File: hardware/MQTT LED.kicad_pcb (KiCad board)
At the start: 2 copper layers, 30 x 40 mm, 21 parts, among them J1 1x2P, J2 1x8P, J3 USB-TYPE-C-009, U1 ESPC2-M1-N2, U2 AL8860QMP-13, U3 AMS1117-3.3

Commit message: added todos
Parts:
- moved D1 6.34 mm to (122.2, 74.1), turned to 0 degrees
- moved L1 4.18 mm to (122.3, 81.3)
- moved R1 1.47 mm to (115.8, 71.4)
- moved J3 1.47 mm to (115.0, 77.5)
- moved R2 1.47 mm to (115.8, 83.5)
- moved C3 1.17 mm to (129.1, 84.4)
- moved U2 1.17 mm to (130.0, 81.5)
- moved R3 1.17 mm to (129.5, 87.1)
- moved J1 0.56 mm to (136.1, 81.0)
- moved C2 0.23 mm to (119.3, 61.8), turned to 90 degrees
- moved C4 0.12 mm to (119.4, 68.2)
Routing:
- net VBUS: track 45.7 -> 35.8 mm
- net +3V3: track 19.0 -> 16.2 mm
- net GND: track 31.0 -> 28.2 mm
- net LED-: track 21.7 -> 19.2 mm
- net LED+: track 9.65 -> 11.4 mm
- net Net-(D1-A): track 11.6 -> 12.5 mm
- net CTRL: track 12.8 -> 13.5 mm

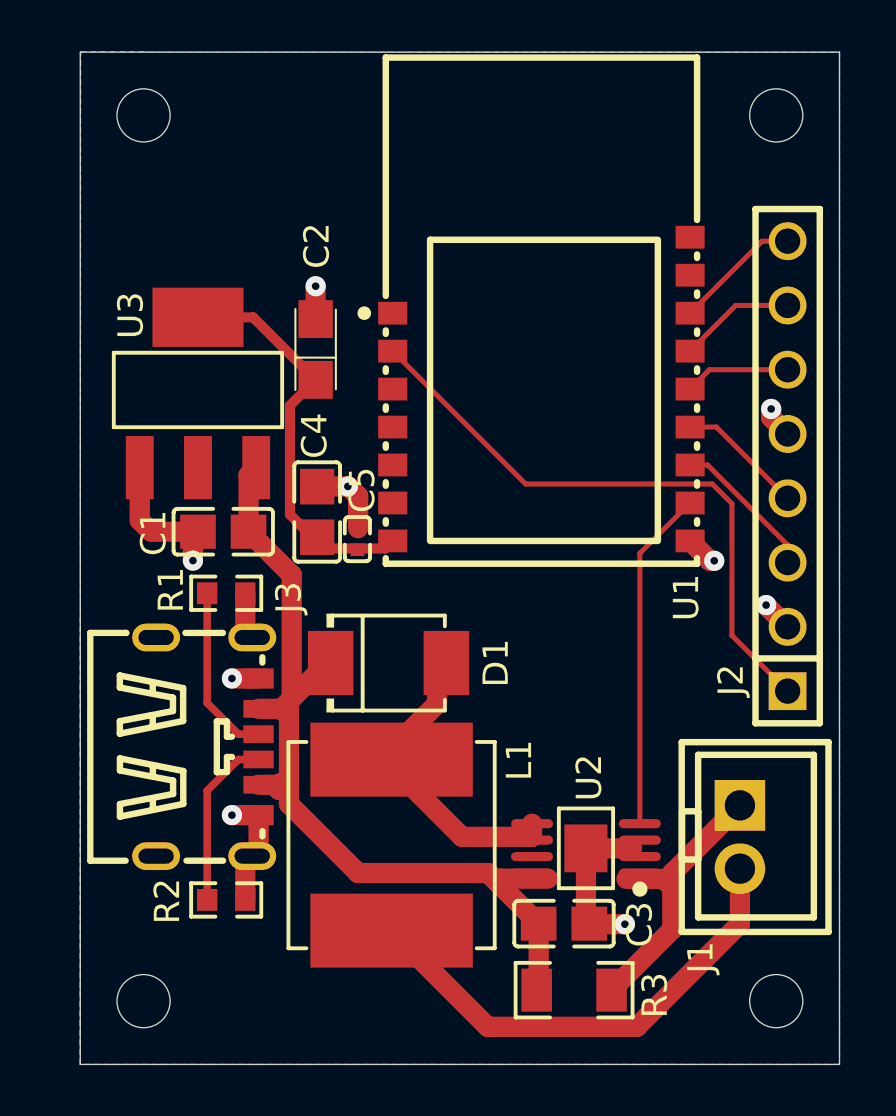
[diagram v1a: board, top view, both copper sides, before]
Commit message: Switched to USB programming and ESP32-C3 module
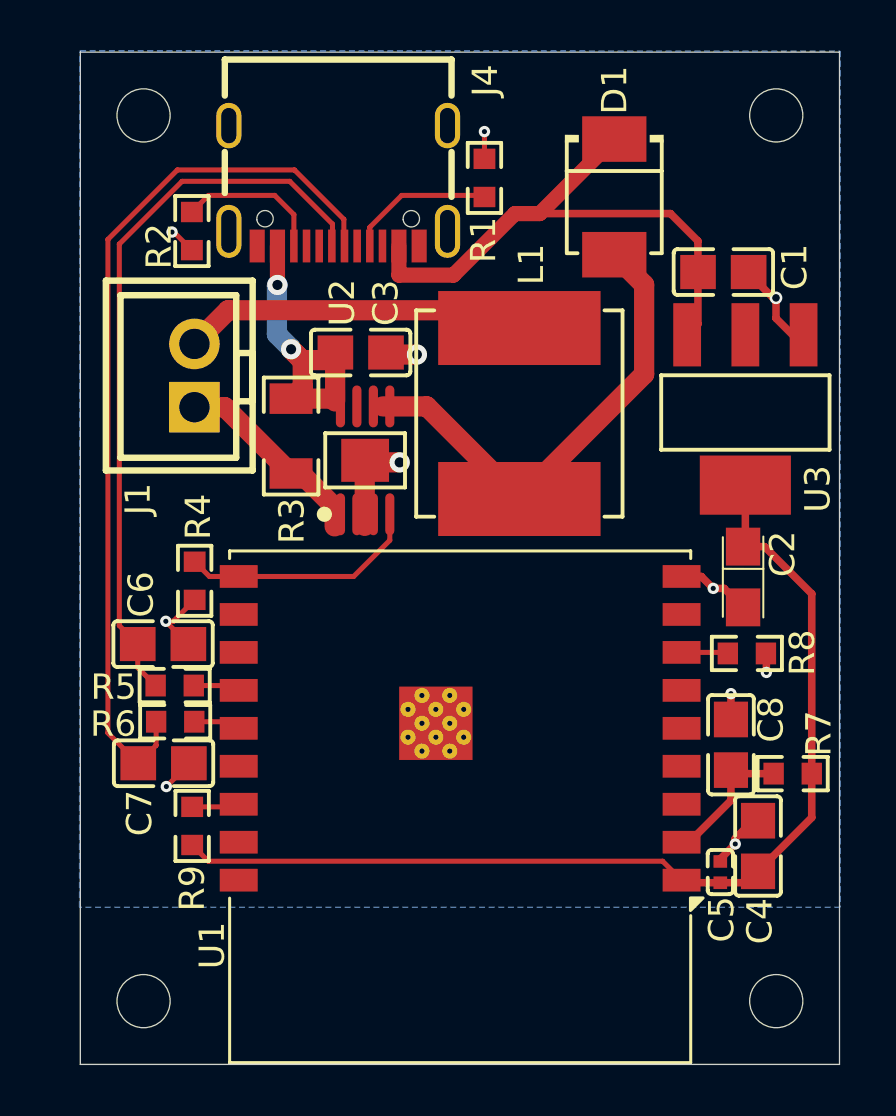
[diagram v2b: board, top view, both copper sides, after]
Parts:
- removed J2: 1x8P, EasyEDA_Lib:HDR-TH_8P-P2.54-V-M-4
- removed J3: USB-TYPE-C-009, EasyEDA_Lib:TYPE-C-SMD_TYPE-C-6P
- added C6: C, EasyEDA_Lib:C0805, F.Cu at (113.3, 73.4)
- added C7: C, EasyEDA_Lib:C0805, F.Cu at (113.3, 78.1)
- added C8: 1uF, EasyEDA_Lib:C0805, F.Cu at (135.7, 77.4)
- added J4: USB_C_Receptacle_USB2.0_16P, EasyEDA_Lib:TYPE-C-SMD_TYPE-C-3.1-16PIN, F.Cu at (120.2, 55.3)
- added R4: 10K, EasyEDA_Lib:R0603, F.Cu at (114.5, 70.9)
- added R5: R, EasyEDA_Lib:R0603, F.Cu at (113.7, 75.0)
- added R6: R, EasyEDA_Lib:R0603, F.Cu at (113.8, 76.5)
- added R7: 10K, EasyEDA_Lib:R0603, F.Cu at (138.2, 78.5)
- added R8: 10K, EasyEDA_Lib:R0603, F.Cu at (136.3, 73.8)
- added R9: 10K, EasyEDA_Lib:R0603, F.Cu at (114.4, 80.6)
- U1: value ESPC2-M1-N2 -> ESP32-C3-WROOM-02; footprint EasyEDA_Lib:WIFIM-SMD_ESPC2-M1 -> RF_Module:ESP32-C3-WROOM-02
- moved J1 28.2 mm to (114.5, 62.8), turned to 90 degrees
- moved R2 26.5 mm to (114.4, 57.1), turned to -90 degrees
- moved R3 24.6 mm to (118.3, 65.2), turned to 90 degrees
- moved C3 24.0 mm to (121.1, 61.9)
- moved C1 22.3 mm to (135.4, 58.7), turned to 180 degrees
- moved C4 21.9 mm to (136.8, 81.4)
- moved U3 21.6 mm to (136.3, 64.1), turned to 90 degrees
- moved D1 20.5 mm to (131.1, 55.7), turned to -90 degrees
- moved C5 19.5 mm to (135.3, 82.4)
- moved R1 19.3 mm to (126.0, 55.0), turned to -90 degrees
- moved C2 19.1 mm to (136.2, 70.7), turned to -90 degrees
- moved L1 17.8 mm to (127.3, 64.3), turned to -90 degrees
- moved U2 17.6 mm to (121.3, 66.1), turned to 0 degrees
- moved U1 13.8 mm to (125.0, 76.7), turned to 180 degrees
- moved G*** 11.5 mm to (125.3, 72.9), turned to 90 degrees
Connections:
- U1 pad 1: unconnected-(U1-IO0-Pad1) -> +3V3
- U1 pad 10: BOOT -> PWM
- U1 pad 11: EXTRA2 -> unconnected-(U1-IO20/RXD-Pad11)
- U1 pad 12: EXTRA1 -> unconnected-(U1-IO21/TXD-Pad12)
- U1 pad 13: RX -> Net-(U1-IO18)
- U1 pad 14: TX -> Net-(U1-IO19)
- U1 pad 16: unconnected-(U1-IO10-Pad16) -> Net-(U1-IO2)
- U1 pad 2: RESET -> Net-(U1-EN)
- U1 pad 7: +3V3 -> Net-(U1-IO8)
- U1 pad 8: GND -> unconnected-(U1-IO9-Pad8)
- U1 pad 9: CTRL -> GND
- U2 pad 4: CTRL -> PWM
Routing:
- net D+: track 0.00 -> 35.5 mm
- net D-: track 0.00 -> 29.1 mm
- net +3V3: track 16.2 -> 41.0 mm
- net RESET: track 24.2 -> 0.00 mm
- net CTRL: track 13.5 -> 0.00 mm
- net PWM: track 0.00 -> 9.57 mm
- net Net-(D1-A): track 12.5 -> 19.1 mm
- net BOOT: track 5.86 -> 0.00 mm
- net GND: track 28.2 -> 22.4 mm, vias 9 -> 11
- net Net-(U1-EN): track 0.00 -> 5.58 mm
- net LED-: track 19.2 -> 13.7 mm
- net TX: track 5.03 -> 0.00 mm
- net EXTRA2: track 5.02 -> 0.00 mm
- net RX: track 4.60 -> 0.00 mm
- net EXTRA1: track 4.17 -> 0.00 mm
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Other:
- board text removed: "BOOT"
- board text removed: "E1"
- board text removed: "E2"
- board text removed: "GND"
- board text removed: "J2"
- board text removed: "RST"
- board text removed: "RX"
- board text removed: "TX"
